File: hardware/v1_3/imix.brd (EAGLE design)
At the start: 87 x 102.5 mm, 154 parts, among them J2_3_5_AND_6 ARDUINO_R3NO_HOLES, U1 BQ2423X, U10 ISL29035, U11 FX0S8700CQ, U12 296-12686-1-ND, U13 SIP32401A, U14 SIP32401A, U15 SIP32401A, U16 SIP32401A, U17 74LVC4066BQ, U18 74LVC4066BQ, U3 TLV3202, U4 LM358, U5 LDO-TPS78233, U6 ATSAM4LCX_100, U8 SI7021, U9 NRF51422, X1 16MHz, X2 16MHz, X3 16MHz

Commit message: Create PDF
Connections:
- net GND: no longer U1.6
- net VCC_IN: now also U1.6
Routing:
- net GND: track 215.8 -> 213.0 mm
- net VCC_IN: track 83.9 -> 85.5 mm
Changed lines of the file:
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@@
 <contactref element="R16" pad="2"/>
 <contactref element="U1" pad="4"/>
-<contactref element="U1" pad="6"/>
 <contactref element="U1" pad="5"/>
 <contactref element="U1" pad="14"/>
@@
 <wire x1="50.747" y1="69.824" x2="50.747" y2="67.247" width="0.1524" layer="1"/>
 <wire x1="50.747" y1="67.247" x2="50.5355" y2="67.0355" width="0.1524" layer="1"/>
-<wire x1="3.025" y1="53.25" x2="4.25" y2="53.25" width="0.1524" layer="1"/>
 <wire x1="4.25" y1="53.25" x2="4.5" y2="53" width="0.1524" layer="1"/>
 <via x="43" y="17.5" extent="1-16" drill="0.3302"/>
@@
 <wire x1="77.5" y1="-3.6" x2="79.65" y2="-3.6" width="0.1524" layer="1"/>
 <wire x1="3" y1="53.775" x2="3.025" y2="53.75" width="0.1524" layer="1"/>
-<wire x1="3.025" y1="53.25" x2="1.75" y2="53.25" width="0.1524" layer="1"/>
-<wire x1="1.75" y1="53.25" x2="1.5" y2="53.5" width="0.1524" layer="1"/>
 <wire x1="3.025" y1="52.25" x2="3.025" y2="51.775" width="0.1524" layer="1"/>
 <wire x1="3.025" y1="51.775" x2="2.5" y2="51.25" width="0.1524" layer="1"/>
@@
 <wire x1="6" y1="50.25" x2="7.5" y2="48.65" width="0" layer="19" extent="1-1"/>
 <wire x1="5.975" y1="52.75" x2="6" y2="50.25" width="0" layer="19" extent="1-1"/>
-<wire x1="3.025" y1="53.75" x2="3.025" y2="53.25" width="0" layer="19" extent="1-1"/>
-<wire x1="3.025" y1="52.25" x2="3.025" y2="53.25" width="0" layer="19" extent="1-1"/>
-<wire x1="3.75" y1="54.475" x2="3.025" y2="53.75" width="0" layer="19" extent="1-1"/>
-<wire x1="1.75" y1="55" x2="1.5" y2="53.5" width="0" layer="19" extent="1-1"/>
+<wire x1="3.75" y1="54.475" x2="4.25" y2="53.25" width="0" layer="19" extent="1-1"/>
+<wire x1="3.025" y1="53.75" x2="3.75" y2="54.475" width="0" layer="19" extent="1-1"/>
+<wire x1="3.025" y1="52.25" x2="3.025" y2="53.75" width="0" layer="19" extent="1-1"/>
+<wire x1="1.75" y1="55" x2="3" y2="53.775" width="0" layer="19" extent="1-1"/>
 <wire x1="9.85" y1="54.5" x2="8" y2="53" width="0" layer="19" extent="1-1"/>
 <wire x1="13.35" y1="54.5" x2="9.85" y2="54.5" width="0" layer="19" extent="1-1"/>
@@
 <wire x1="-27.4" y1="-35.5" x2="-24.65" y2="-36.225" width="0" layer="19" extent="1-1"/>
 <wire x1="-27.65" y1="-36.225" x2="-27.4" y2="-35.5" width="0" layer="19" extent="1-1"/>
-<wire x1="-18.55" y1="-43.15" x2="-24.65" y2="-36.225" width="0" layer="19" extent="1-1"/>
+<wire x1="-18.55" y1="-43.15" x2="-18.65" y2="-36.225" width="0" layer="19" extent="1-1"/>
 <wire x1="-20.1" y1="-43.4" x2="-18.55" y2="-43.15" width="0" layer="19" extent="1-1"/>
 <wire x1="-24.85" y1="-45.55" x2="-20.1" y2="-43.4" width="0" layer="19" extent="1-1"/>
@@
 <wire x1="8.5" y1="24.5" x2="9.505" y2="23.495" width="0.4064" layer="1"/>
 <wire x1="9.505" y1="23.495" x2="9.505" y2="23.06" width="0.4064" layer="1"/>
+<contactref element="U1" pad="6"/>
+<wire x1="3.025" y1="53.25" x2="1.75" y2="53.25" width="0.1524" layer="1"/>
+<wire x1="1.75" y1="53.25" x2="1.5" y2="53.5" width="0.1524" layer="1"/>
+<wire x1="5.975" y1="52.25" x2="3.025" y2="53.25" width="0" layer="19" extent="1-1"/>
 </signal>
 <signal name="N$47">

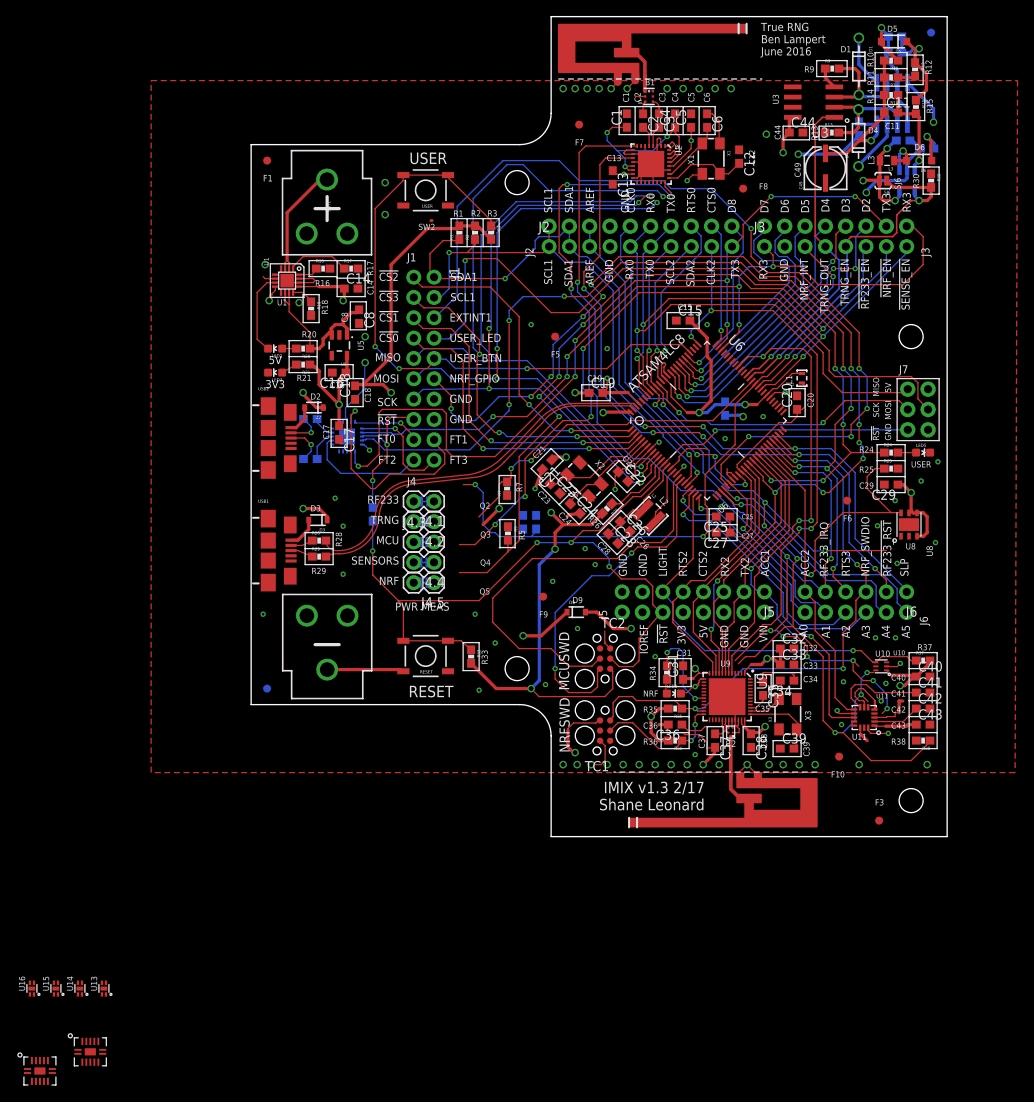
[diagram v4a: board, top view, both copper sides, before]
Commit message: Eliminated FabDoc layers and migrated all components to imix library
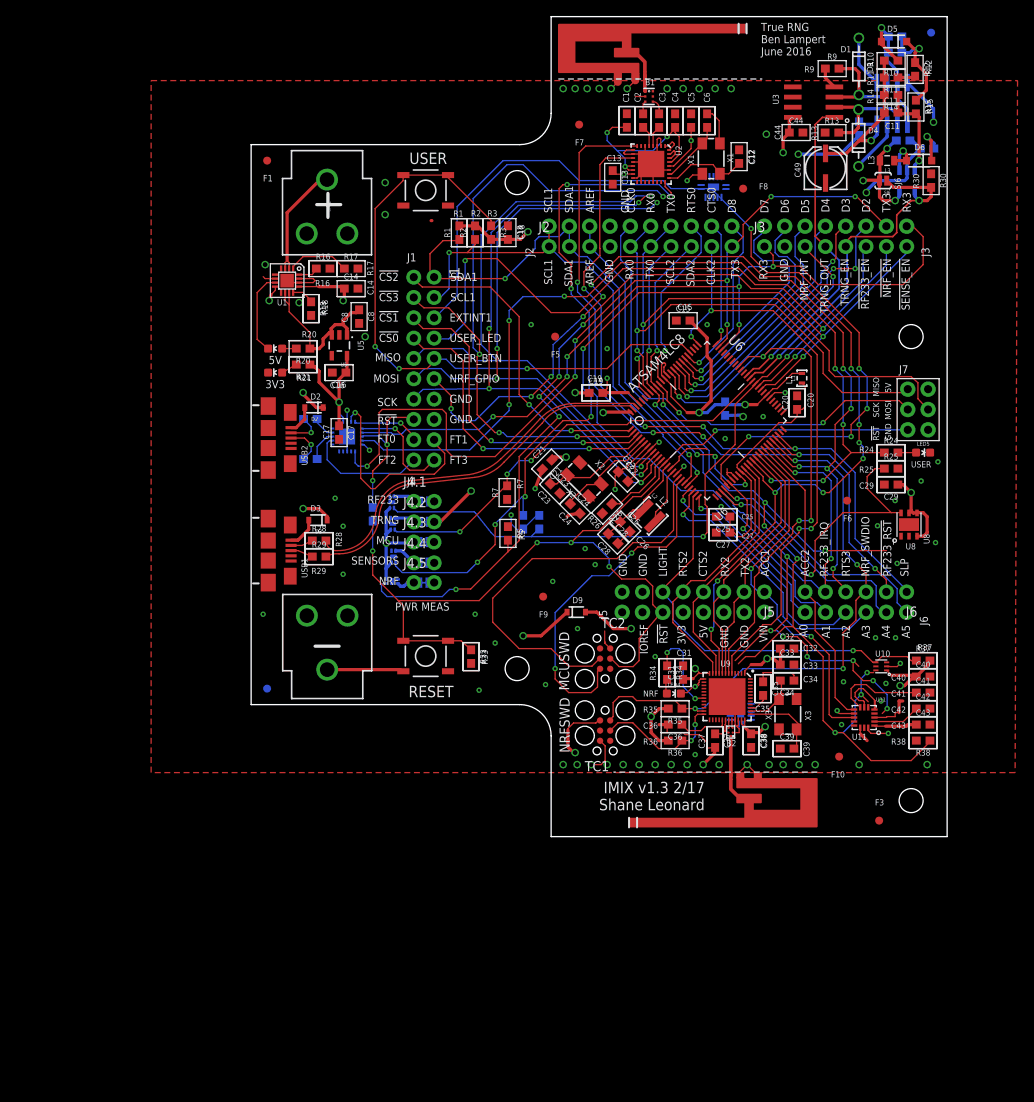
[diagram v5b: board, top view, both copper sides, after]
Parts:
- removed RESET, USER: (no value), SparkFun-Retired:TACTILE-SWITCH-SMD
- added SW1, SW2: TAC_SWITCHSMD, imix:TACTILE-SWITCH-SMD
- B1: device stanford_iot_research:BALUN0805 -> imix:BALUN0805
- B2: device stanford_iot_research:BAL_NRF01D3 -> imix:BAL_NRF01D3
- BAT1: device imix_v1:BATTERY_18650-HOLDER -> imix:BATTERY_18650-HOLDER
- C17: device rcl:C0603 -> imix:C0603
- D1, D4: device SparkFun-DiscreteSemi:DIODE-ZENER -> imix:DIODE-ZENER
- D2, D3, D9: value NSR1020MW2T3G -> 250mA/100V; device SparkFun-DiscreteSemi:SOD-323 -> imix:SOD-323
- D5: device SparkFun-DiscreteSemi:SOD-123 -> imix:SOD-123
- D6: device imix_v1:SOD-123 -> imix:SOD-123
- F1, F10, F2, F3, F4, F5, F6, F7, F8, F9: device GeekAmmo:FIDUCIAL -> imix:FIDUCIAL
- J1: device SparkFun-Connectors:2X10_ROUND_NOSILK -> imix:2X10_ROUND_NOSILK
- J2: device SparkFun-Connectors:1X10_NO_SILK -> imix:1X10_NO_SILK
- J3, J5: device SparkFun-Connectors:1X08_NO_SILK -> imix:1X08_NO_SILK
- J4.1, J4.2, J4.3, J4.4, J4.5: device SparkFun-Connectors:1X02 -> imix:1X02_NO_SILK
- J6: device SparkFun-Connectors:1X06_NO_SILK -> imix:1X06_NO_SILK
- L1: device stanford_iot_research:L0603 -> imix:L0603
- L2: device stanford_iot_research:L1212 -> imix:L1212
- L3: device SparkFun-Passives:0805 -> imix:0805
- LED2: value 5V -> BLUE; device SparkFun-LED:LED-0603 -> imix:LED-0603
- LED3: value 3.3V -> BLUE; device SparkFun-LED:LED-0603 -> imix:LED-0603
- LED4: value NRF -> BLUE; device SparkFun-LED:LED-0603 -> imix:LED-0603
- LED5: value USER -> BLUE; device SparkFun-LED:LED-0603 -> imix:LED-0603
- TC1, TC2: device TagConnect:TC2030-IDC -> imix:TC2030-IDC
- U12, U5: device SparkFun-PowerIC:SOT23-5 -> imix:SOT23-5
- U2: device stanford_iot_research:32QN2 -> imix:32QN2
- U3, U4: device analog-devices:SO8 -> imix:SO8
- U7: device stanford_iot_research:QFN20 -> imix:QFN20
- USB1, USB2: device SparkFun-Connectors-Fixed:USB-AB-MICRO-SMD -> imix:USB-AB-MICRO-SMD
- X1, X2, X3: device stanford_iot_research:CTS_405_SERIES -> imix:CTS_405_SERIES
- moved U17 133.2 mm to (57.8, 64.7), flipped to the bottom
- moved U18 98.4 mm to (61.2, -0.90), flipped to the bottom, turned to 90 degrees
- moved U15 73.9 mm to (17.6, 25.3), flipped to the bottom, turned to 180 degrees
- moved U16 73.6 mm to (17.7, 22.6), flipped to the bottom, turned to 180 degrees
- moved U13 65.0 mm to (17.8, 18.5), flipped to the bottom, turned to 180 degrees
- moved U14 64.1 mm to (17.6, 15.4), flipped to the bottom, turned to 270 degrees
- moved C18 27.7 mm to (32.1, 59.0), turned to 270 degrees
- moved J4.4 2.52 mm to (20.3, 17.7), turned to 0 degrees
- moved J4.2 2.52 mm to (20.3, 22.8), turned to 0 degrees
- moved J4.5 2.52 mm to (20.3, 15.3), turned to 0 degrees
- moved J4.1 2.52 mm to (20.3, 25.4), turned to 0 degrees
- moved R7 0.50 mm to (32.0, 26.5)
- moved R6 0.40 mm to (36.0, 22.8)
- turned SJ1 to 0 degrees
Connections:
- net !RESET: now also SW1.3, SW1.4; no longer RESET.3, RESET.4
- net GND: now also SW1.1, SW1.2, SW2.1, SW2.2; no longer RESET.1, RESET.2, USER.1, USER.2
- net USER_BTN: now also SW2.3, SW2.4; no longer USER.3, USER.4
- net VCC_NRF_3V3: now also J4.5.2, SJ2.2
- net VCC_RF233_3V3: no longer J4.5.2, SJ2.2
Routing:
- net VCC_MCU_3V3: track 188.3 -> 77.8 mm, vias 10 -> 7
- net VCC_NRF_3V3: track 32.4 -> 52.1 mm
- net VCC_3V3: track 23.9 -> 39.4 mm, vias 2 -> 3
- net SENSE_PWR_EN: track 96.5 -> 110.3 mm, vias 6 -> 7
- net NRF_PWR_EN: track 103.0 -> 115.7 mm, vias 6 -> 7
- net TRNG_PWR_EN: track 42.8 -> 53.8 mm, vias 2 -> 3
- net RF233_PWR_EN: track 81.4 -> 87.0 mm, vias 3 -> 2
- net N$8: track 0.00 -> 3.67 mm
- net N$33: track 0.00 -> 3.59 mm
- net N$32: track 0.00 -> 3.40 mm
- net N$18: track 0.00 -> 3.10 mm
- net GND: track 213.0 -> 211.5 mm, vias 84 -> 85
- net VCC_SENSE_3V3: track 27.0 -> 27.7 mm
- net VCC_RF233_3V3: track 9.05 -> 9.76 mm
- net FTDI1: track 26.6 -> 25.9 mm
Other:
- board text added: "IMIX v1.3 Mar 2017 Shane Leonard"
- board text removed: "BATT CLIP"
- board text removed: "DNP"
- board text removed: "IMIX v1.2 Oct 2016 Shane Leonard"
- board text removed: "IMIX v1.3 Feb 2017 Shane Leonard"
- board text removed: "LED2"
- board text removed: "LED3"
- board text removed: "LED4"
- board text removed: "LED5"
- board text removed: "Q2"
- board text removed: "Q3"
- board text removed: "Q4"
- board text removed: "Q5"
- board text removed: "SW1"
- board text removed: "SW2"
- board text removed: "USB1"
- board text removed: "USB2"

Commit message: Only 19 airwires to go
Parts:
- moved R38 34.4 mm to (66.8, 25.2), flipped to the bottom
- moved R25 34.3 mm to (50.8, 47.5), flipped to the bottom, turned to 90 degrees
- moved U18 32.6 mm to (80.3, 25.6), turned to 180 degrees
- moved C29 20.1 mm to (76.5, 7.75), flipped to the bottom, turned to 0 degrees
- moved U8 16.8 mm to (78.2, 6.24), turned to 180 degrees
- moved C41 9.76 mm to (74.2, 2.00), turned to 90 degrees
- moved C43 9.58 mm to (74.5, -3.75), flipped to the bottom, turned to 90 degrees
- moved C40 7.40 mm to (76.8, 2.00), flipped to the bottom, turned to 270 degrees
- moved R37 7.25 mm to (76.8, 5.25), flipped to the bottom
- moved C15 7.19 mm to (53.5, 40.8), flipped to the bottom, turned to 315 degrees
- moved C42 5.20 mm to (79.8, -3.50), turned to 270 degrees
- moved U10 2.89 mm to (76.7, 2.72), turned to 0 degrees
- moved F8 2.68 mm to (63.9, 65.7)
- moved C50 2.33 mm to (60.0, 39.2), turned to 315 degrees
- moved U17 1.20 mm to (59.0, 64.7), turned to 180 degrees
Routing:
- net SENSE_TWI_SCL: track 0.00 -> 50.2 mm, vias 0 -> 2
- net TWI2_SDA: track 127.5 -> 80.3 mm, vias 9 -> 6
- net SENSE_TWI_SDA: track 0.00 -> 38.8 mm, vias 0 -> 1
- net SENSE_PWR_EN: track 110.3 -> 148.4 mm, vias 7 -> 9
- net NRF_TWI_SCL: track 0.00 -> 36.7 mm, vias 0 -> 1
- net NRF_PWR_EN: track 115.7 -> 151.3 mm, vias 7 -> 9
- net NRF_TWI_SDA: track 0.00 -> 34.0 mm, vias 0 -> 1
- net TWI2_SCL: track 116.1 -> 83.9 mm, vias 10 -> 5
- net VCC_MCU_3V3: track 77.8 -> 58.9 mm, vias 7 -> 12
- net SCK: track 78.7 -> 95.4 mm, vias 4 -> 5
- net RF233_MOSI: track 0.00 -> 16.2 mm, vias 0 -> 1
- net RF233_CS: track 0.00 -> 13.9 mm, vias 0 -> 1
- net GND: track 211.5 -> 223.3 mm, vias 85 -> 87
- net MOSI: track 77.5 -> 88.7 mm, vias 4 -> 3
- net SPI_NCS3: track 88.2 -> 98.9 mm, vias 4 -> 3
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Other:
- board text removed: "C40"

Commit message: Down to 6 airwires
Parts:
- moved X1 3.35 mm to (55.5, 70.9), flipped to the bottom, turned to 180 degrees
- moved C1 3.23 mm to (46.7, 69.8), flipped to the bottom
- moved C12 2.75 mm to (59.5, 70.8), flipped to the bottom
- moved C6 2.69 mm to (54.4, 73.7), flipped to the bottom, turned to 0 degrees
- moved F8 1.32 mm to (65.2, 65.9)
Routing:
- net RF233_PWR_EN: track 91.0 -> 125.1 mm, vias 2 -> 4
- net RF233_SCK: track 0.00 -> 25.8 mm, vias 0 -> 1
- net RF233_MISO: track 0.00 -> 12.4 mm, vias 0 -> 1
- net GND: track 223.3 -> 234.7 mm, vias 87 -> 94
- net VCC_MCU_3V3: track 58.9 -> 68.3 mm, vias 12 -> 13
- net N$2: track 23.9 -> 17.5 mm, vias 3 -> 2
- net MOSI: track 88.7 -> 91.3 mm
- net RF233_MOSI: track 16.2 -> 13.8 mm
- net N$4: track 7.99 -> 10.3 mm, vias 0 -> 1
- net RF233_IRQ: track 109.1 -> 107.6 mm
- net RF233_CS: track 13.9 -> 15.0 mm
- net SPI_NCS3: track 98.9 -> 99.9 mm
- net VCC_TRNG_3V3: track 116.0 -> 115.0 mm
- net N$40: track 10.6 -> 9.59 mm, vias 0 -> 1
- net SCK: track 95.4 -> 94.7 mm
